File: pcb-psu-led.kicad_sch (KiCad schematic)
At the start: 6 parts, among them J1 MAINS INPUT 230V, T1 Talema 70000K, U1 LM78L05ACZ

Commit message: ECAD-14: add primary fuse F1 rated T32 mA per Talema datasheet
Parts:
- added F1: T32mA 250V, symbol PSU_LED:Fuse
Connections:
- net L_SW: now also F1.1; no longer T1.6 (P1_START)
- new net L_FUSED: F1.2, T1.6 (P1_START)
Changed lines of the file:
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@@
   )
   (wire
-    (pts (xy 83.82 100.33) (xy 83.82 93.98))
-    (stroke
-      (width 0)
-      (type default)
-    )
-  )
-  (wire
-    (pts (xy 83.82 93.98) (xy 93.98 93.98))
+    (pts (xy 83.82 100.33) (xy 83.82 86.36))
     (stroke
       (width 0)
@@
       (width 0)
       (type default)
+    )
+  )
+  (wire
+    (pts (xy 93.98 86.36) (xy 93.98 93.98))
+    (stroke
+      (width 0)
+      (type default)
+    )
+  )
+  (label "L_FUSED"
+    (at 93.98 90.17 90)
+    (effects
+      (font (size 1.27 1.27))
     )
   )
@@
     )
   )
+  (symbol
+    (lib_id "PSU_LED:Fuse")
+    (at 88.9 86.36 0)
+    (unit 1)
+    (exclude_from_sim no)
+    (in_bom yes)
+    (on_board yes)
+    (dnp no)
+    (fields_autoplaced yes)
+    (property "Reference" "F1"
+      (at 88.9 83.82 0)
+      (effects
+        (font (size 1.27 1.27))
+      )
+    )
+    (property "Value" "T32mA 250V"
+      (at 88.9 88.9 0)
+      (effects
+        (font (size 1.27 1.27))
+      )
+    )
+    (property "Footprint" ""
+      (at 88.9 86.36 0)
+      (effects
+        (font (size 1.27 1.27))
+        (hide yes)
+      )
+    )
+    (property "Datasheet" ""
+      (at 88.9 86.36 0)
+      (effects
+        (font (size 1.27 1.27))
+        (hide yes)
+      )
+    )
+    (property "Description" "Primary fuse T32 mA 250 V time-lag; Talema 700xxK 230V Fuse (Max.) = 32 mA for 1.6 VA"
+      (at 88.9 86.36 0)
+      (effects
+        (font (size 1.27 1.27))
+        (hide yes)
+      )
+    )
+    (property "Manufacturer" ""
+      (at 88.9 86.36 0)
+      (effects
+        (font (size 1.27 1.27))
+        (hide yes)
+      )
+    )
+    (property "MPN" "TBD"
+      (at 88.9 86.36 0)
+      (effects
+        (font (size 1.27 1.27))
+        (hide yes)
+      )
+    )
+    (pin "1"
+    )
+    (pin "2"
+    )
+    (instances
+      (project "pcb-psu-led"
+        (path "/a08e89e5-29a6-4ee5-b521-7a214388ab56"
+          (reference "F1")
+          (unit 1)
+        )
+      )
+    )
+  )

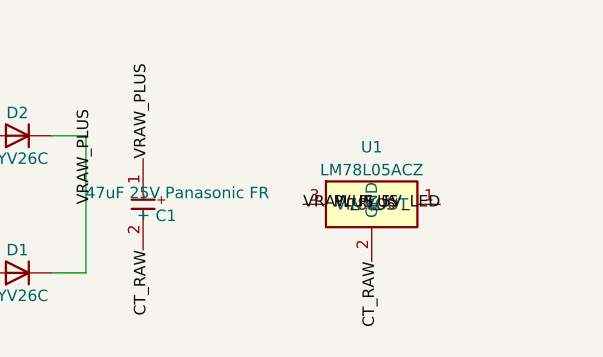
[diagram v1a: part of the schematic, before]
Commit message: ECAD-15: add U1 input and output bypass capacitors C2 and C3
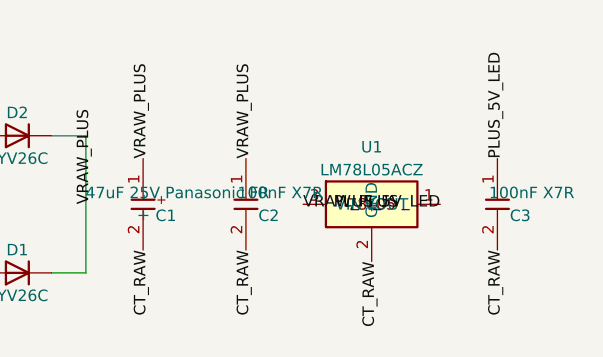
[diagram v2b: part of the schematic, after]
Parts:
- added C2, C3: 100nF X7R, symbol PSU_LED:C
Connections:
- net CT_RAW: now also C2.2, C3.2
- net PLUS_5V_LED: now also C3.1
- net VRAW_PLUS: now also C2.1
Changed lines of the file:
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@@
+    )
+  )
+  (label "VRAW_PLUS"
+    (at 146.05 96.52 90)
+    (effects
+      (font (size 1.27 1.27))
+    )
+  )
+  (label "CT_RAW"
+    (at 146.05 106.68 270)
+    (effects
+      (font (size 1.27 1.27))
+    )
+  )
+  (label "PLUS_5V_LED"
+    (at 173.99 96.52 90)
+    (effects
+      (font (size 1.27 1.27))
+    )
+  )
+  (label "CT_RAW"
+    (at 173.99 106.68 270)
+    (effects
+      (font (size 1.27 1.27))
     )
   )
@@
           (unit 1)
         )
+      )
+    )
+  )
+  (symbol
+    (lib_id "PSU_LED:C")
+    (at 146.05 101.6 0)
+    (unit 1)
+    (exclude_from_sim no)
+    (in_bom yes)
+    (on_board yes)
+    (dnp no)
+    (fields_autoplaced no)
+    (property "Reference" "C2"
+      (at 148.59 102.86999999999999 0)
+      (effects
+        (font (size 1.27 1.27))
+      )
+    )
+    (property "Value" "100nF X7R"
+      (at 149.86 100.33 0)
+      (effects
+        (font (size 1.27 1.27))
+      )
+    )
+    (property "Footprint" ""
+      (at 146.05 101.6 0)
+      (effects
+        (font (size 1.27 1.27))
+        (hide yes)
+      )
+    )
+    (property "Datasheet" ""
+      (at 146.05 101.6 0)
+      (effects
+        (font (size 1.27 1.27))
+        (hide yes)
+      )
+    )
+    (property "Description" "Input bypass for U1, 100 nF X7R, Rev. 6.4.1 item E-08"
+      (at 146.05 101.6 0)
+      (effects
+        (font (size 1.27 1.27))
+        (hide yes)
+      )
+    )
+    (property "Manufacturer" ""
+      (at 146.05 101.6 0)
+      (effects
+        (font (size 1.27 1.27))
+        (hide yes)
+      )
+    )
+    (property "MPN" "TBD"
+      (at 146.05 101.6 0)
+      (effects
+        (font (size 1.27 1.27))
+        (hide yes)
+      )
+    )
+    (pin "1"
+    )
+    (pin "2"
+    )
+    (instances
+      (project "pcb-psu-led"
+        (path "/a08e89e5-29a6-4ee5-b521-7a214388ab56"
+          (reference "C2")
+          (unit 1)
+        )
+      )
+    )
+  )
+  (symbol
+    (lib_id "PSU_LED:C")
+    (at 173.99 101.6 0)
+    (unit 1)
+    (exclude_from_sim no)
+    (in_bom yes)
+    (on_board yes)
+    (dnp no)
+    (fields_autoplaced no)
+    (property "Reference" "C3"
+      (at 176.53 102.86999999999999 0)
+      (effects
+        (font (size 1.27 1.27))
+      )
+    )
+    (property "Value" "100nF X7R"
+      (at 177.8 100.33 0)
+      (effects
+        (font (size 1.27 1.27))
+      )
+    )
+    (property "Footprint" ""
+      (at 173.99 101.6 0)
+      (effects
+        (font (size 1.27 1.27))
+        (hide yes)
+      )
+    )
+    (property "Datasheet" ""
+      (at 173.99 101.6 0)
+      (effects
+        (font (size 1.27 1.27))
+        (hide yes)
+      )
+    )
+    (property "Description" "Output bypass for U1, 100 nF X7R, Rev. 6.4.1 item E-08"
+      (at 173.99 101.6 0)
+      (effects
+        (font (size 1.27 1.27))
+        (hide yes)
+      )
+    )
+    (property "Manufacturer" ""
+      (at 173.99 101.6 0)
+      (effects
+        (font (size 1.27 1.27))
+        (hide yes)
+      )
+    )
+    (property "MPN" "TBD"
+      (at 173.99 101.6 0)
+      (effects
+        (font (size 1.27 1.27))
+        (hide yes)
+      )
+    )
+    (pin "1"
+    )
+    (pin "2"
+    )
+    (instances
+      (project "pcb-psu-led"
+        (path "/a08e89e5-29a6-4ee5-b521-7a214388ab56"
+          (reference "C3")
+          (unit 1)
+        )

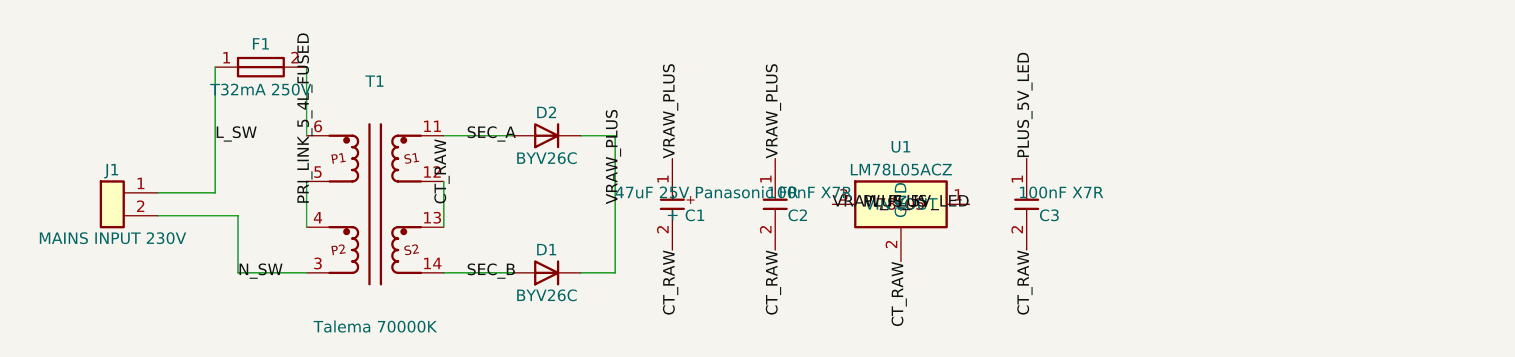
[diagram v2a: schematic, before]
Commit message: ECAD-16: add LED branch R1, RV1 and output connector J2
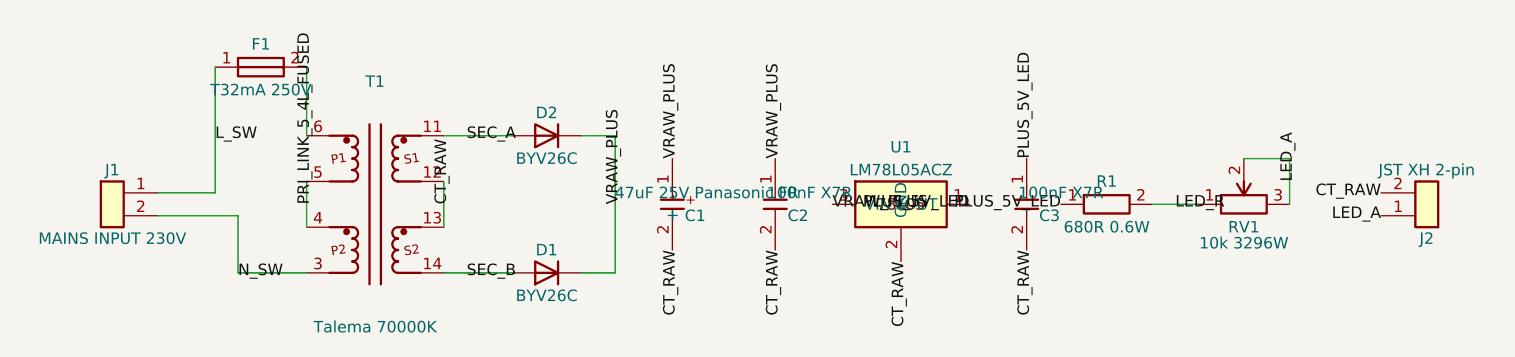
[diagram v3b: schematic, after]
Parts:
- added J2: JST XH 2-pin, symbol PSU_LED:Conn_01x02
- added R1: 680R 0.6W, symbol PSU_LED:R
- added RV1: 10k 3296W, symbol PSU_LED:R_Potentiometer
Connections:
- net CT_RAW: now also J2.2 (Pin_2)
- net PLUS_5V_LED: now also R1.1
- new net LED_A: J2.1 (Pin_1), RV1.2, RV1.3
- new net LED_R: R1.2, RV1.1

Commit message: ECAD-19b: actually assign footprints to schematic instances
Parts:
- C1: footprint (none) -> PSU_LED:CP_Radial_D6.3mm_P2.50mm
- C2, C3: footprint (none) -> PSU_LED:C_Disc_D5.0mm_W2.5mm_P5.00mm
- D1, D2: footprint (none) -> PSU_LED:D_DO-15_P12.70mm_Horizontal
- F1: footprint (none) -> PSU_LED:Fuseholder_Cylinder-5x20mm_Schurter_FUP_0031.2510_Horizontal_Closed
- J1: footprint (none) -> PSU_LED:TerminalBlock_Phoenix_MKDS-1,5-2-5.08_1x02_P5.08mm_Horizontal
- J2: footprint (none) -> PSU_LED:JST_XH_S2B-XH-A_1x02_P2.50mm_Horizontal
- R1: footprint (none) -> PSU_LED:R_Axial_DIN0309_L9.0mm_D3.2mm_P12.70mm_Horizontal
- RV1: footprint (none) -> PSU_LED:Potentiometer_Bourns_3296W_Vertical
- U1: footprint (none) -> PSU_LED:TO-92_Wide
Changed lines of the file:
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@@
       )
     )
-    (property "Footprint" ""
+    (property "Footprint" "PSU_LED:Fuseholder_Cylinder-5x20mm_Schurter_FUP_0031.2510_Horizontal_Closed"
       (at 88.9 86.36 0)
       (effects
@@
       )
     )
-    (property "Footprint" ""
+    (property "Footprint" "PSU_LED:C_Disc_D5.0mm_W2.5mm_P5.00mm"
       (at 146.05 101.6 0)
       (effects
@@
       )
     )
-    (property "Footprint" ""
+    (property "Footprint" "PSU_LED:C_Disc_D5.0mm_W2.5mm_P5.00mm"
       (at 173.99 101.6 0)
       (effects
@@
       )
     )
-    (property "Footprint" ""
+    (property "Footprint" "PSU_LED:R_Axial_DIN0309_L9.0mm_D3.2mm_P12.70mm_Horizontal"
       (at 182.88 101.6 0)
       (effects
@@
       )
     )
-    (property "Footprint" ""
+    (property "Footprint" "PSU_LED:Potentiometer_Bourns_3296W_Vertical"
       (at 198.12 101.6 0)
       (effects
@@
       )
     )
-    (property "Footprint" ""
+    (property "Footprint" "PSU_LED:JST_XH_S2B-XH-A_1x02_P2.50mm_Horizontal"
       (at 218.44 101.6 0)
       (effects
@@
       )
     )
-    (property "Footprint" ""
+    (property "Footprint" "PSU_LED:TerminalBlock_Phoenix_MKDS-1,5-2-5.08_1x02_P5.08mm_Horizontal"
       (at 72.39 101.6 0)
       (effects
@@
       (effects (font (size 1.27 1.27)))
     )
-    (property "Footprint" ""
+    (property "Footprint" "PSU_LED:D_DO-15_P12.70mm_Horizontal"
       (at 120.65 93.98 0)
       (effects
@@
       (effects (font (size 1.27 1.27)))
     )
-    (property "Footprint" ""
+    (property "Footprint" "PSU_LED:D_DO-15_P12.70mm_Horizontal"
       (at 120.65 109.22 0)
       (effects
@@
       )
     )
-    (property "Footprint" ""
+    (property "Footprint" "PSU_LED:TO-92_Wide"
       (at 160.02 101.6 0)
       (effects
@@
       )
     )
-    (property "Footprint" ""
+    (property "Footprint" "PSU_LED:CP_Radial_D6.3mm_P2.50mm"
       (at 134.62 101.6 0)
       (effects
